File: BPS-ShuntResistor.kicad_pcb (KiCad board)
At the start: 2 copper layers, 40.1 x 35.1 mm, 15 parts, among them J3 Amp_Conn

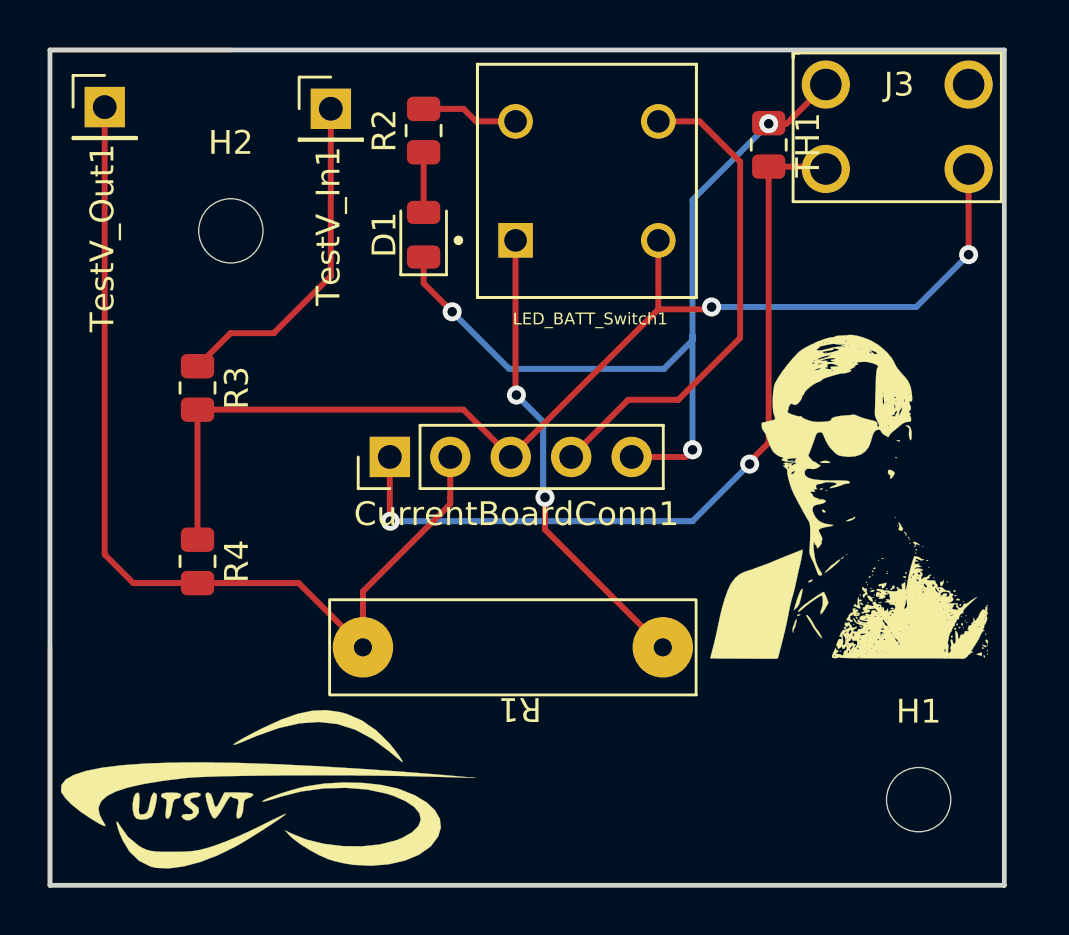
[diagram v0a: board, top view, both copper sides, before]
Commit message: switch footprint is invalid agony
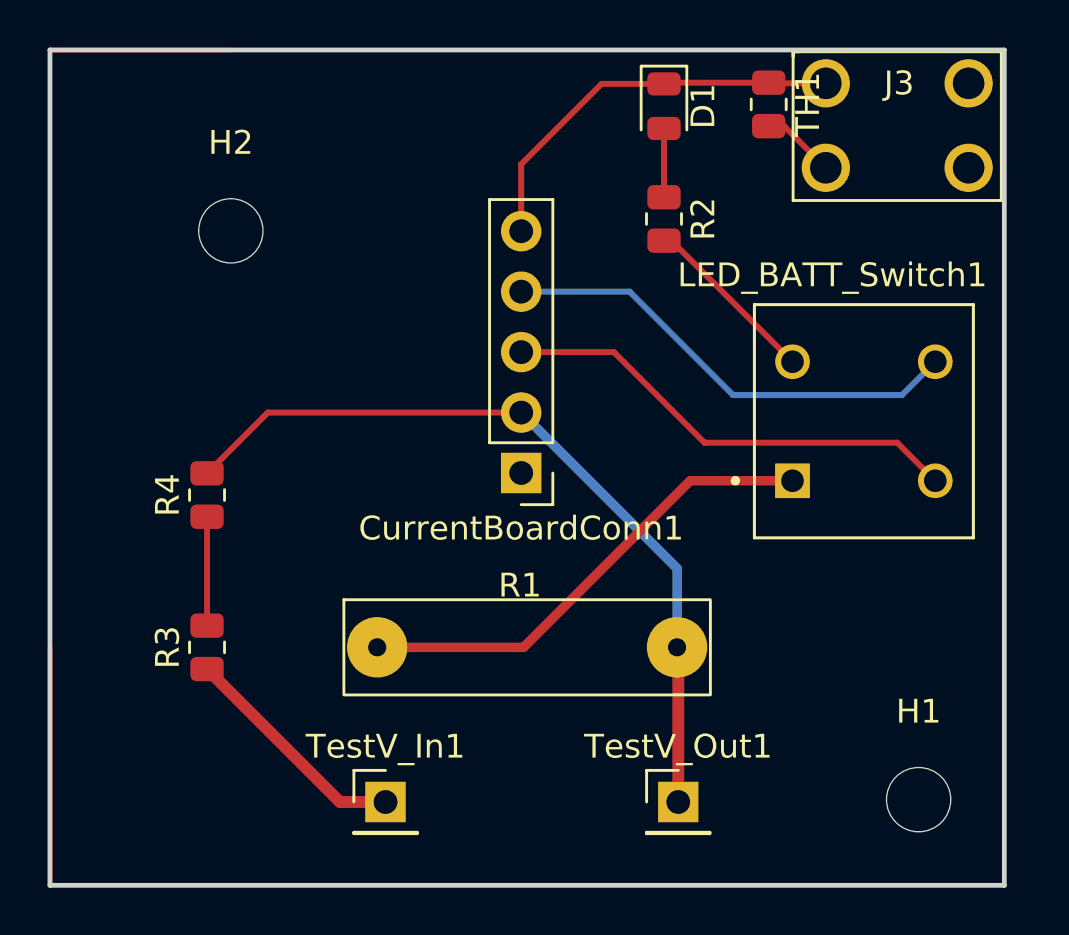
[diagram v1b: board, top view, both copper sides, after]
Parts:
- LOGO1, LOGO2: moved to B.Cu
- moved TestV_Out1 37.9 mm to (143.8, 116.1)
- moved LOGO1 29.5 mm to (136.9, 88.2), turned to 180 degrees
- moved TestV_In1 29.2 mm to (131.5, 116.1)
- moved LOGO2 27.2 mm to (124.6, 111.3), turned to 180 degrees
- moved LED_BATT_Switch1 15.4 mm to (151.6, 100.1)
- moved D1 11.5 mm to (143.2, 86.9), turned to -90 degrees
- moved R3 10.9 mm to (124.0, 109.6), turned to 90 degrees
- moved R2 10.8 mm to (143.2, 91.6), turned to -90 degrees
- moved CurrentBoardConn1 5.56 mm to (137.2, 102.3), turned to 180 degrees
- moved R4 2.82 mm to (124.0, 103.2), turned to 90 degrees
- moved TH1 1.70 mm to (147.6, 86.8)
- turned R1 to 0 degrees
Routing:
- net ETS: track 34.1 -> 3.12 mm, vias 2 -> 0
- net RSHH: track 48.7 -> 24.2 mm, vias 2 -> 0
- net GND: track 35.4 -> 17.0 mm, vias 3 -> 0
- net RSHL: track 40.8 -> 33.4 mm
- net Net-(R3-Pad1): track 14.2 -> 9.81 mm
- net Net-(LED_BATT_Switch1-Pad3): track 4.08 -> 7.51 mm
- net +3V3: track 20.7 -> 19.8 mm
- net Net-(LED_BATT_Switch1-Pad1): track 19.7 -> 20.3 mm, vias 2 -> 0

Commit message: working on it
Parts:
- removed LED_BATT_Switch1: SW_DPST, UTSVT_Passive:SW_PVA1EEH1
- added SW1: SW_DPST, UTSVT_Special:SDDJE32700, F.Cu at (150.5, 99.2)
- LOGO1, LOGO2: moved to F.Cu
- moved LOGO2 69.4 mm to (190.8, 90.5), turned to 0 degrees
- moved LOGO1 33.9 mm to (170.8, 87.3), turned to 0 degrees
- moved D1 22.3 mm to (149.3, 108.3), turned to 0 degrees
- moved R2 20.4 mm to (154.9, 108.3), turned to 0 degrees
- moved R4 1.02 mm to (125.0, 103.0)
- moved R3 1.00 mm to (125.0, 109.6)
- moved TestV_Out1 1.00 mm to (143.8, 115.1)
- moved TestV_In1 0.89 mm to (131.1, 115.3)
- moved TH1 0.70 mm to (146.9, 86.8)
- moved CurrentBoardConn1 0.67 mm to (137.5, 102.9)
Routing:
- net GND: track 17.0 -> 49.3 mm, vias 0 -> 2
- net RSHH: track 24.2 -> 31.7 mm
- net Net-(R1-Pad1): track 20.3 -> 17.1 mm
- net Net-(R2-Pad2): track 7.51 -> 4.27 mm
- net RSHL: track 33.4 -> 30.6 mm
- net Net-(R3-Pad1): track 9.81 -> 8.09 mm
- net ETS: track 3.12 -> 4.63 mm
- net Net-(D1-Pad2): track 2.89 -> 3.72 mm

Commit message: version 1 of the pcb redesign
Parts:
- moved H2 40.9 mm to (162.3, 109.0)
- moved LOGO1 40.7 mm to (208.1, 71.2)
- moved LOGO2 40.7 mm to (228.2, 74.4)
- moved H1 37.1 mm to (133.3, 85.1)
- moved R2 27.1 mm to (130.4, 96.7), turned to -90 degrees
- moved D1 25.6 mm to (130.4, 91.1), turned to -90 degrees
- moved R4 23.8 mm to (148.3, 107.4), turned to 0 degrees
- moved R3 18.9 mm to (143.8, 107.4), turned to 0 degrees
- moved CurrentBoardConn1 18.5 mm to (145.4, 86.1), turned to 0 degrees
- moved TestV_In1 11.6 mm to (139.6, 107.4)
- moved TestV_Out1 11.3 mm to (152.1, 107.5)
- moved R1 10.9 mm to (145.5, 102.5)
- moved SW1 10.4 mm to (158.4, 92.4)
- moved J3 8.68 mm to (159.8, 82.1)
- moved TH1 8.20 mm to (153.7, 82.2)
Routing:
- net Net-(R2-Pad2): track 4.27 -> 33.9 mm, vias 0 -> 1
- net RSHH: track 31.7 -> 52.3 mm, vias 0 -> 2
- net RSHL: track 30.6 -> 44.0 mm, vias 0 -> 2
- net ETS: track 4.63 -> 13.1 mm
- net GND: track 49.3 -> 43.2 mm
- net Net-(R3-Pad1): track 8.09 -> 3.30 mm
- net Net-(R1-Pad1): track 17.1 -> 16.5 mm
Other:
- board size 40.1 x 35.1 mm -> 37.6 x 32.5 mm
- board text added: "GND 3V3 RSHH RSHL ETS"

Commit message: still working on layout.
i want to double check some footprints.
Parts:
- added TP1: TestPoint, TestPoint:TestPoint_Keystone_5005-5009_Compact, F.Cu at (111.7, 99.2)
- added TP2: TestPoint, TestPoint:TestPoint_Keystone_5005-5009_Compact, F.Cu at (111.7, 93.5)
- added TP3: TestPoint, TestPoint:TestPoint_Keystone_5005-5009_Compact, F.Cu at (111.8, 88.2)
- moved LOGO2 49.7 mm to (179.5, 84.3)
- moved LOGO1 47.0 mm to (161.2, 72.0)
- moved D1 22.1 mm to (116.0, 107.8), turned to 180 degrees
- moved R2 21.9 mm to (111.0, 106.8), turned to 90 degrees
- moved TH1 17.5 mm to (136.2, 82.3)
- moved CurrentBoardConn1 17.4 mm to (128.0, 85.6)
- moved TestV_In1 17.4 mm to (122.2, 109.2)
- moved TestV_Out1 17.3 mm to (134.8, 109.2)
- moved H2 17.3 mm to (145.0, 109.0)
- moved H1 17.3 mm to (116.0, 85.0)
- moved R4 17.3 mm to (131.2, 109.2)
- moved R1 17.2 mm to (128.2, 102.6)
- moved R3 17.2 mm to (126.7, 109.2)
- moved J3 17.2 mm to (142.6, 82.0)
- moved SW1 16.6 mm to (141.8, 92.8)
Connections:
- CurrentBoardConn1 pad 2: RSHL -> RSHH
- CurrentBoardConn1 pad 3: RSHH -> RSHL
- CurrentBoardConn1 pad 4: +3V3 -> GND
- CurrentBoardConn1 pad 5: GND -> +3V3
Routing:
- net +3V3: track 20.0 -> 39.3 mm
- net RSHH: track 52.3 -> 62.7 mm
- net Net-(R2-Pad2): track 33.9 -> 40.3 mm
- net GND: track 43.2 -> 39.2 mm
- net ETS: track 13.1 -> 16.0 mm
- net RSHL: track 44.0 -> 41.6 mm, vias 2 -> 0
- net Net-(R1-Pad1): track 16.5 -> 17.1 mm
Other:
- board size 37.6 x 32.5 mm -> 40.1 x 35.1 mm
- board text added: "3V3 GND RSHL RSHH ETS"
- board text added: "Copyright (c) 2022-2023 Longhorn Solar Shunt Resistor Board"
- board text removed: "GND 3V3 RSHH RSHL ETS"

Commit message: updating custom board parts
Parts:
- SW1: footprint UTSVT_Special:SDDJE32700 -> UTSVT_Special:206212
- moved SW1 17.0 mm to (158.8, 93.1), turned to 0 degrees
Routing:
- net RSHH: track 62.7 -> 43.9 mm
- net +3V3: track 39.3 -> 25.4 mm
- net Net-(R1-Pad1): track 17.1 -> 6.40 mm
- net Net-(R2-Pad2): track 40.3 -> 30.4 mm
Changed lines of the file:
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@@
     )
   )
-  (footprint "UTSVT_Special:SDDJE32700" (layer "F.Cu")
-    (at 141.825 92.8 90)
-    (property "Sheetfile" "BPS-ShuntResistor.kicad_sch")
-    (property "Sheetname" "")
-    (attr through_hole)
-    (fp_text reference "SW1" (at 0 0 90) (layer "F.SilkS")
-      (effects (font (size 0.787402 0.787402) (thickness 0.15)))
-    )
-    (fp_text value "SW_DPST" (at 0 0 90) (layer "F.Fab")
-      (effects (font (size 0.787402 0.787402) (thickness 0.15)))
-    )
-    (pad "1" thru_hole circle (at -5.25 -4.375 90) (size 2.25 2.25) (drill 1.5) (layers *.Cu *.Mask)
-      (net 7 "Net-(R1-Pad1)") (pinfunction "1") (pintype "passive"))
-    (pad "2" thru_hole circle (at 5 -4.375 90) (size 2.25 2.25) (drill 1.5) (layers *.Cu *.Mask)
-      (net 3 "RSHH") (pinfunction "2") (pintype "passive"))
-    (pad "3" thru_hole circle (at -5.25 4.375 90) (size 2.25 2.25) (drill 1.5) (layers *.Cu *.Mask)
-      (net 8 "Net-(R2-Pad2)") (pinfunction "3") (pintype "passive"))
-    (pad "4" thru_hole circle (at 5 4.375 90) (size 2.25 2.25) (drill 1.5) (layers *.Cu *.Mask)
-      (net 4 "+3V3") (pinfunction "4") (pintype "passive"))
-  )
   (footprint "Connector_PinHeader_2.54mm:PinHeader_1x01_P2.54mm_Vertical" (layer "F.Cu")
     (at 122.25 109.2)
@@
     (pad "" np_thru_hole circle (at 0 0) (size 2.7 2.7) (drill 2.7) (layers *.Cu *.Mask))
   )
+  (footprint "UTSVT_Special:206212" (layer "F.Cu")
+    (at 158.85 93.1)
+    (descr "206-212-1")
+    (tags "Switch")
+    (property "Sheetfile" "BPS-ShuntResistor.kicad_sch")
+    (property "Sheetname" "")
+    (attr through_hole)
+    (fp_text reference "SW1" (at 3.81 3.455) (layer "F.SilkS")
+      (effects (font (size 1.27 1.27) (thickness 0.254)))
+    )
+    (fp_text value "SW_DPST" (at 3.81 3.455) (layer "F.SilkS") hide
+      (effects (font (size 1.27 1.27) (thickness 0.254)))
+    )
+    (fp_text user "${REFERENCE}" (at 3.81 3.455) (layer "F.Fab")
+      (effects (font (size 1.27 1.27) (thickness 0.254)))
+    )
+    (fp_line (start 0.11 -1.69) (end 0.11 -1.69) (layer "F.SilkS") (width 0.2))
+    (fp_line (start -2.36 8.7) (end -2.36 -1.08) (layer "F.SilkS") (width 0.1))
+    (fp_line (start -0.09 -1.69) (end -0.09 -1.69) (layer "F.SilkS") (width 0.2))
+    (fp_line (start 9.98 8.7) (end -2.36 8.7) (layer "F.SilkS") (width 0.1))
+    (fp_line (start 9.98 -1.08) (end 9.98 8.7) (layer "F.SilkS") (width 0.1))
+    (fp_line (start -2.36 -1.08) (end 9.98 -1.08) (layer "F.SilkS") (width 0.1))
+    (fp_arc (start -0.09 -1.69) (mid 0.01 -1.79) (end 0.11 -1.69) (layer "F.SilkS") (width 0.2))
+    (fp_arc (start 0.11 -1.69) (mid 0.01 -1.59) (end -0.09 -1.69) (layer "F.SilkS") (width 0.2))
+    (fp_line (start -2.86 9.2) (end -2.86 -2.29) (layer "F.CrtYd") (width 0.1))
+    (fp_line (start 10.48 9.2) (end -2.86 9.2) (layer "F.CrtYd") (width 0.1))
+    (fp_line (start 10.48 -2.29) (end 10.48 9.2) (layer "F.CrtYd") (width 0.1))
+    (fp_line (start -2.86 -2.29) (end 10.48 -2.29) (layer "F.CrtYd") (width 0.1))
+    (fp_line (start 9.98 8.7) (end -2.36 8.7) (layer "F.Fab") (width 0.2))
+    (fp_line (start 9.98 -1.08) (end 9.98 8.7) (layer "F.Fab") (width 0.2))
+    (fp_line (start -2.36 8.7) (end -2.36 -1.08) (layer "F.Fab") (width 0.2))
+    (fp_line (start -2.36 -1.08) (end 9.98 -1.08) (layer "F.Fab") (width 0.2))
+    (pad "A1" thru_hole circle locked (at 0 0) (size 1.381 1.381) (drill 0.85) (layers *.Cu *.Mask))
+    (pad "A2" thru_hole circle locked (at 2.54 0) (size 1.381 1.381) (drill 0.85) (layers *.Cu *.Mask))
+    (pad "A3" thru_hole circle locked (at 5.08 0) (size 1.381 1.381) (drill 0.85) (layers *.Cu *.Mask))
+    (pad "A4" thru_hole circle locked (at 7.62 0) (size 1.381 1.381) (drill 0.85) (layers *.Cu *.Mask))
+    (pad "B1" thru_hole circle locked (at 0 7.62) (size 1.381 1.381) (drill 0.85) (layers *.Cu *.Mask))
+    (pad "B2" thru_hole circle locked (at 2.54 7.62) (size 1.381 1.381) (drill 0.85) (layers *.Cu *.Mask))
+    (pad "B3" thru_hole circle locked (at 5.08 7.62) (size 1.381 1.381) (drill 0.85) (layers *.Cu *.Mask))
+    (pad "B4" thru_hole circle locked (at 7.62 7.62) (size 1.381 1.381) (drill 0.85) (layers *.Cu *.Mask))
+    (model "206-212.stp"
+      (offset (xyz 0 0 0))
+      (scale (xyz 1 1 1))
+      (rotate (xyz 0 0 0))
+    )
+  )
   (footprint "TestPoint:TestPoint_Keystone_5005-5009_Compact" (layer "F.Cu")
     (at 111.7 93.55)
@@
     )
   )
-  (gr_rect (start 136 86.25) (end 147.75 99.55) (layer "F.SilkS") (width 0.2) (fill none))
   (gr_rect (start 108.49 77.47) (end 148.59 112.57) (layer "Edge.Cuts") (width 0.2) (fill none))
   (gr_text "Copyright (c) 2022-2023 Longhorn Solar\nShunt Resistor Board" (at 123.15 80) (layer "F.SilkS")
@@
   (segment (start 127.575 109.2) (end 127.575 102.475) (width 0.25) (layer "F.Cu") (net 3))
   (segment (start 128.34 87.8) (end 128 88.14) (width 0.25) (layer "F.Cu") (net 3))
-  (segment (start 137.45 87.8) (end 141.823 87.8) (width 0.25) (layer "F.Cu") (net 3))
   (segment (start 123.95 88.15) (end 127.99 88.15) (width 0.25) (layer "F.Cu") (net 3))
   (segment (start 127.99 88.15) (end 128 88.14) (width 0.25) (layer "F.Cu") (net 3))
   (segment (start 111.8 88.15) (end 123.95 88.15) (width 0.25) (layer "F.Cu") (net 3))
-  (segment (start 137.45 87.8) (end 128.34 87.8) (width 0.25) (layer "F.Cu") (net 3))
   (segment (start 127.575 102.475) (end 122.45 97.35) (width 0.25) (layer "F.Cu") (net 3))
-  (segment (start 141.823 87.8) (end 145.6 84.023) (width 0.25) (layer "F.Cu") (net 3))
   (segment (start 127.575 109.2) (end 130.25 109.2) (width 0.25) (layer "F.Cu") (net 3))
   (via (at 122.45 97.35) (size 0.8) (drill 0.4) (layers "F.Cu" "B.Cu") (net 3))
@@
   (segment (start 121.35 95.75) (end 121.36 95.76) (width 0.25) (layer "F.Cu") (net 4))
   (segment (start 121.36 95.76) (end 128 95.76) (width 0.25) (layer "F.Cu") (net 4))
-  (segment (start 143.6 87.8) (end 146.2 87.8) (width 0.25) (layer "B.Cu") (net 4))
   (segment (start 128 95.76) (end 135.64 95.76) (width 0.25) (layer "B.Cu") (net 4))
-  (segment (start 138.8 92.6) (end 143.6 87.8) (width 0.25) (layer "B.Cu") (net 4))
-  (segment (start 135.64 95.76) (end 138.8 92.6) (width 0.25) (layer "B.Cu") (net 4))
   (segment (start 137.0875 80.475) (end 136.175 81.3875) (width 0.25) (layer "F.Cu") (net 5))
   (segment (start 131.6 85.9625) (end 136.175 81.3875) (width 0.25) (layer "F.Cu") (net 5))
@@
   (segment (start 111 107.75) (end 115.0625 107.75) (width 0.25) (layer "F.Cu") (net 6))
   (segment (start 126.775 98.05) (end 122.25 102.575) (width 0.25) (layer "B.Cu") (net 7))
-  (segment (start 137.45 98.05) (end 126.775 98.05) (width 0.25) (layer "B.Cu") (net 7))
   (segment (start 111.025 105.9) (end 111 105.925) (width 0.25) (layer "F.Cu") (net 8))
   (segment (start 113.35 105.9) (end 111.025 105.9) (width 0.25) (layer "F.Cu") (net 8))
   (via (at 113.35 105.9) (size 0.8) (drill 0.4) (layers "F.Cu" "B.Cu") (net 8))
-  (segment (start 141.35 105.95) (end 146.2 101.1) (width 0.25) (layer "B.Cu") (net 8))
   (segment (start 141.35 105.95) (end 113.4 105.95) (width 0.25) (layer "B.Cu") (net 8))
-  (segment (start 146.2 101.1) (end 146.2 98.05) (width 0.25) (layer "B.Cu") (net 8))
   (segment (start 113.4 105.95) (end 113.35 105.9) (width 0.25) (layer "B.Cu") (net 8))
   (segment (start 122.25 109.2) (end 125.75 109.2) (width 0.25) (layer "F.Cu") (net 9))

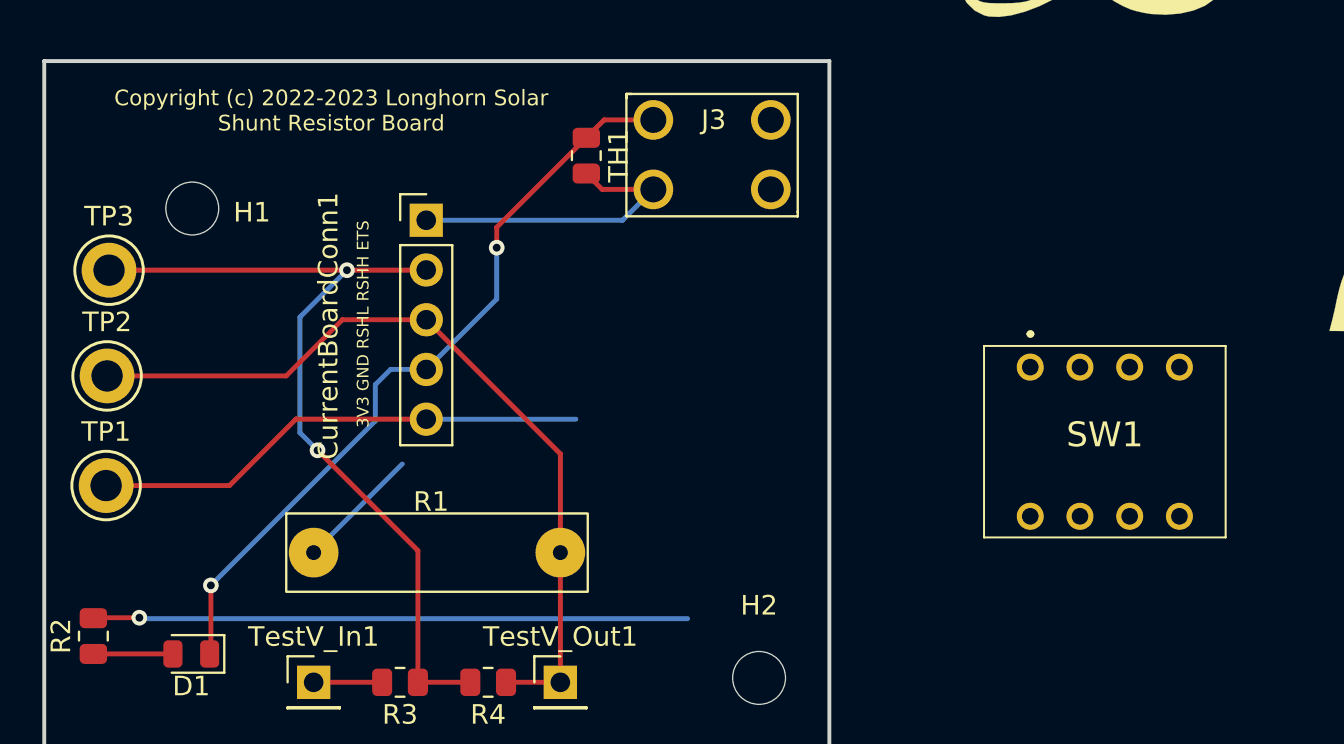
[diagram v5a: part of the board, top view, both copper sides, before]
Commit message: added new switch, updated board and schematic
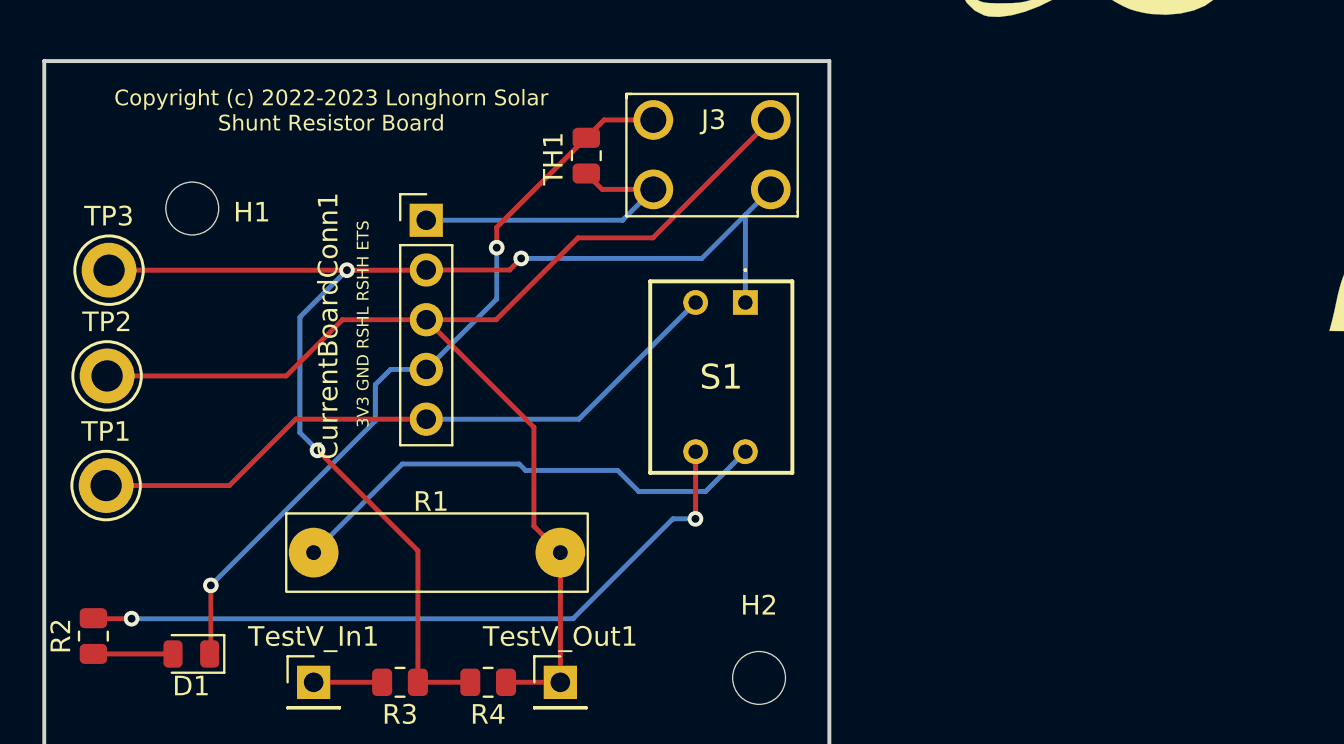
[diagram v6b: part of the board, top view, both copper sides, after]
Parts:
- removed SW1: SW_DPST, UTSVT_Special:206212
- added S1: 206-211S, custom footprints:206211S, F.Cu at (144.3, 89.8)
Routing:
- net RSHH: track 43.9 -> 67.2 mm, vias 2 -> 3
- net RSHL: track 41.6 -> 63.4 mm
- net Net-(R1-Pad1): track 6.40 -> 25.3 mm
- net +3V3: track 25.4 -> 34.0 mm
- net Net-(R2-Pad2): track 30.4 -> 36.3 mm, vias 1 -> 2

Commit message: reworking w tianda on sat
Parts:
- moved TP2 99.5 mm to (206.3, 63.0)
- moved TestV_In1 86.5 mm to (199.2, 69.7)
- moved D1 86.2 mm to (195.7, 74.8), turned to 0 degrees
- moved R4 83.0 mm to (203.7, 68.9)
- moved R3 81.7 mm to (200.1, 73.5)
- moved R2 79.5 mm to (188.0, 86.8), turned to 0 degrees
- moved TP1 78.5 mm to (188.5, 82.8)
- moved H1 74.4 mm to (190.0, 76.8)
- moved H2 71.4 mm to (200.3, 63.9)
- moved TP3 66.9 mm to (178.6, 85.1)
- moved CurrentBoardConn1 60.6 mm to (184.2, 62.8)
- moved TH1 59.7 mm to (195.7, 77.8), turned to 0 degrees
- moved TestV_Out1 54.3 mm to (183.4, 84.9)
- moved R1 53.6 mm to (171.4, 70.7)
- moved S1 50.0 mm to (190.5, 70.7), turned to 0 degrees
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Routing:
- net RSHH: track 67.2 -> 0.00 mm, vias 3 -> 0
- net RSHL: track 63.4 -> 0.00 mm
- net GND: track 39.2 -> 0.00 mm, vias 2 -> 0
- net Net-(R2-Pad2): track 36.3 -> 0.00 mm, vias 2 -> 0
- net +3V3: track 34.0 -> 0.00 mm
- net Net-(R1-Pad1): track 25.3 -> 0.00 mm
- net ETS: track 16.0 -> 0.00 mm
- net Net-(D1-Pad2): track 4.06 -> 0.00 mm
- net Net-(R3-Pad1): track 3.50 -> 0.00 mm
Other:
- board text removed: "3V3 GND RSHL RSHH ETS"
- board text removed: "Copyright (c) 2022-2023 Longhorn Solar Shunt Resistor Board"
